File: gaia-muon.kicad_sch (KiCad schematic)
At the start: 88 parts, among them J1 Debug_Conn, J2 Conn_02x10_Odd_Even, J3 Conn_02x10_Odd_Even, J4 Conn_01x04_Pin, Q1 2N7002, SW1 SW_Push, U1 TPH2502, U2 TPH2502, U3 MAX5026, U4 LM4040DBZ-2.5, U5 MICROFC-60035-SIPM, U6 RP2040, U7 AP2112K-3.3, U8 W25Q128JVS, Y1 AMB8-272-T3

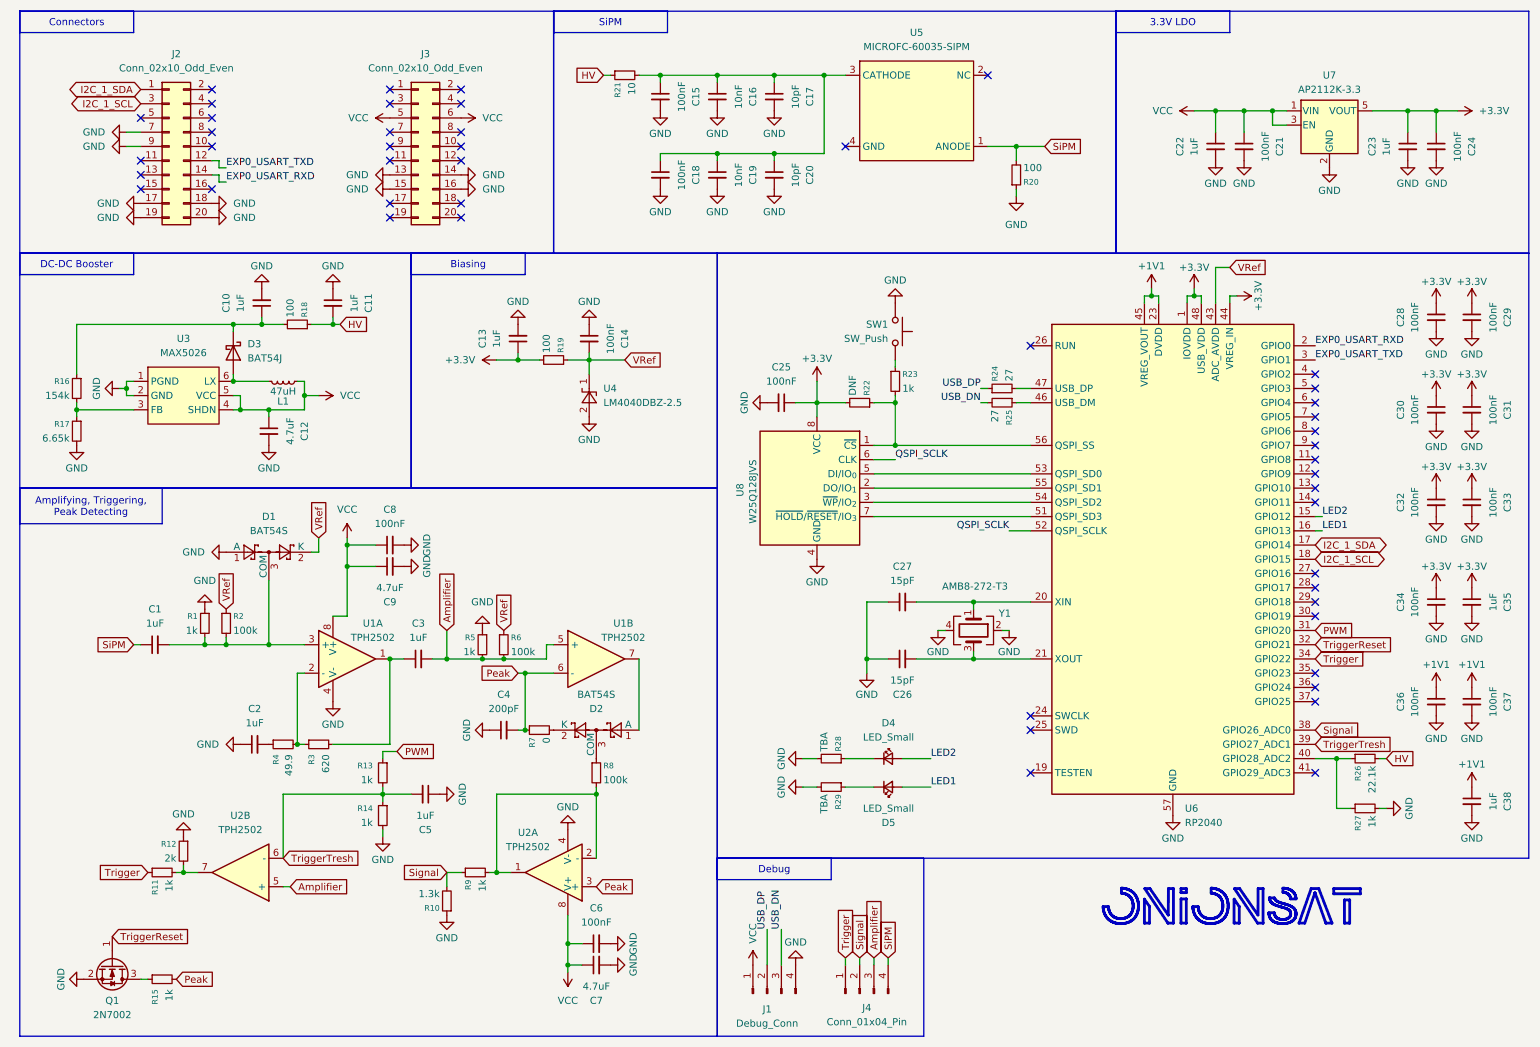
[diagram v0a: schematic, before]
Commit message: placing components, start routing
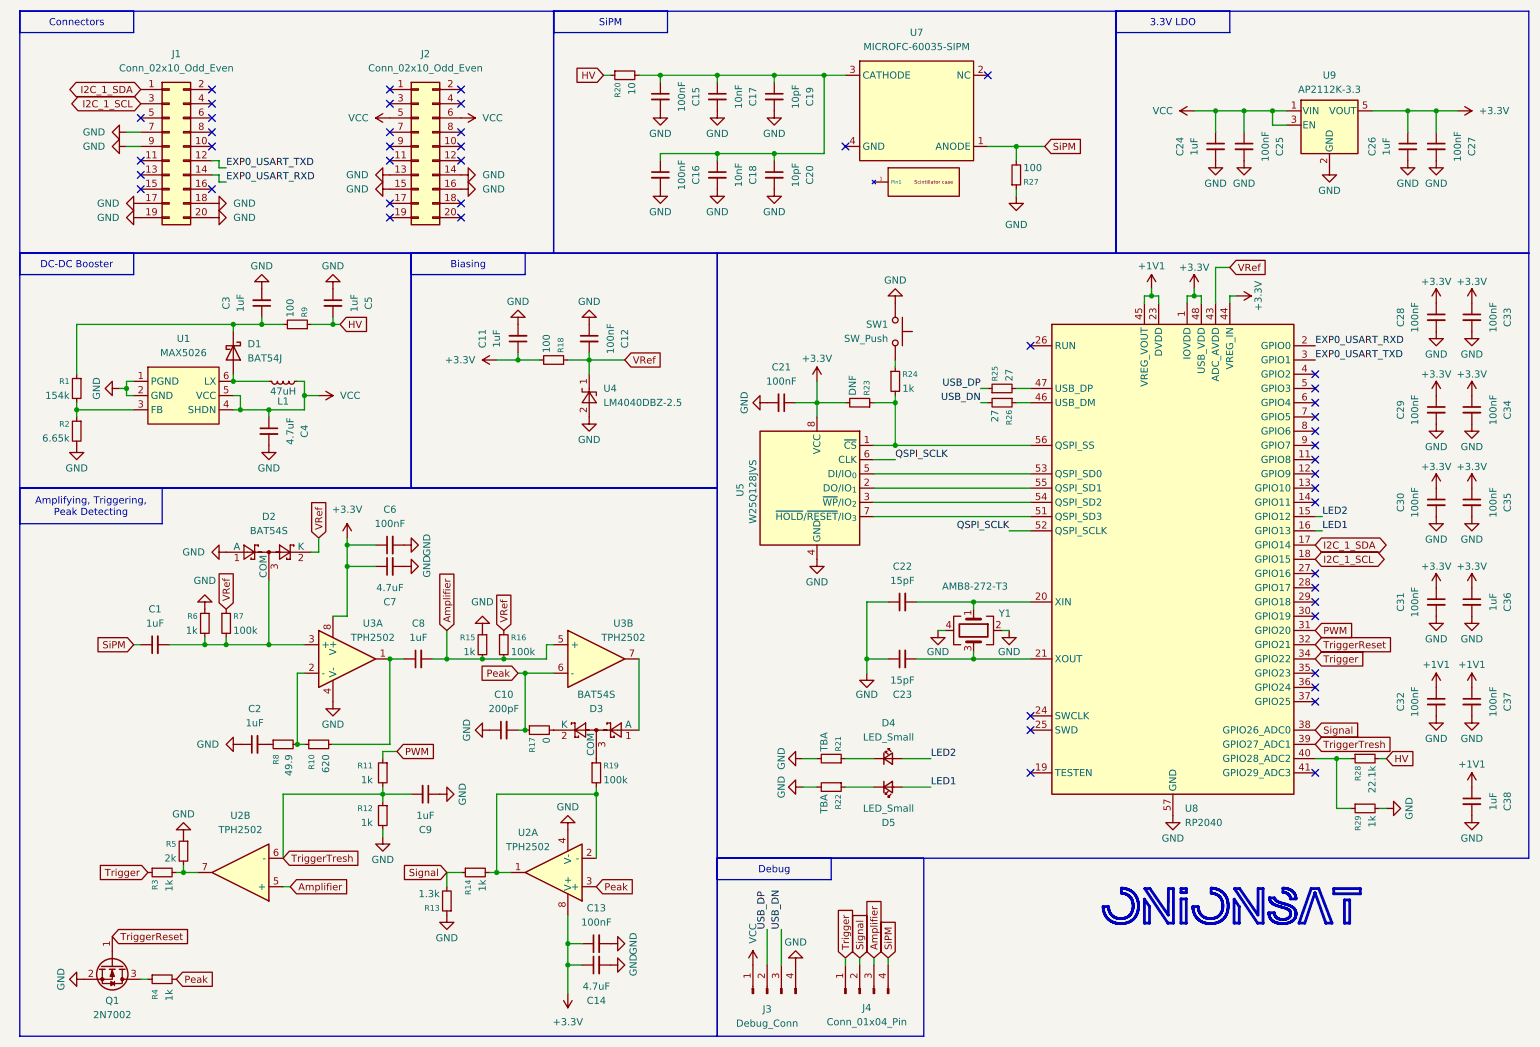
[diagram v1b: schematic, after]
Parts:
- added U6: ~, gaia-muon-footprints:scintillator-case, symbol gaia-muon-symbols:scintillator-case
- C1, C15, C2, C20: footprint (none) -> Capacitor_SMD:C_0805_2012Metric
- C10: renamed from C4; footprint (none) -> Capacitor_SMD:C_0805_2012Metric
- C11: renamed from C13; footprint (none) -> Capacitor_SMD:C_0805_2012Metric
- C12: renamed from C14; footprint (none) -> Capacitor_SMD:C_0805_2012Metric
- C13: renamed from C6; footprint (none) -> Capacitor_SMD:C_0402_1005Metric
- C14: renamed from C7; footprint (none) -> Capacitor_SMD:C_0402_1005Metric
- C16: renamed from C18; footprint (none) -> Capacitor_SMD:C_0805_2012Metric
- C17: renamed from C16; footprint (none) -> Capacitor_SMD:C_0805_2012Metric
- C18: renamed from C19; footprint (none) -> Capacitor_SMD:C_0805_2012Metric
- C19: renamed from C17; footprint (none) -> Capacitor_SMD:C_0805_2012Metric
- C21: renamed from C25; footprint (none) -> Capacitor_SMD:C_0805_2012Metric
- C22: renamed from C27; footprint (none) -> Capacitor_SMD:C_0402_1005Metric
- C23: renamed from C26; footprint (none) -> Capacitor_SMD:C_0402_1005Metric
- C24: renamed from C22; footprint (none) -> Capacitor_SMD:C_0603_1608Metric
- C25: renamed from C21; footprint (none) -> Capacitor_SMD:C_0603_1608Metric
- C26: renamed from C23; footprint (none) -> Capacitor_SMD:C_0603_1608Metric
- C27: renamed from C24; footprint (none) -> Capacitor_SMD:C_0603_1608Metric
- C28, C37, C38: footprint (none) -> Capacitor_SMD:C_0402_1005Metric
- C29: renamed from C30; footprint (none) -> Capacitor_SMD:C_0402_1005Metric
- C3: renamed from C10; footprint (none) -> Capacitor_SMD:C_0805_2012Metric
- C30: renamed from C32; footprint (none) -> Capacitor_SMD:C_0402_1005Metric
- C31: renamed from C34; footprint (none) -> Capacitor_SMD:C_0402_1005Metric
- C32: renamed from C36; footprint (none) -> Capacitor_SMD:C_0402_1005Metric
- C33: renamed from C29; footprint (none) -> Capacitor_SMD:C_0402_1005Metric
- C34: renamed from C31; footprint (none) -> Capacitor_SMD:C_0402_1005Metric
- C35: renamed from C33; footprint (none) -> Capacitor_SMD:C_0402_1005Metric
- C36: renamed from C35; footprint (none) -> Capacitor_SMD:C_0402_1005Metric
- C4: renamed from C12; footprint (none) -> Capacitor_SMD:C_0805_2012Metric
- C5: renamed from C11; footprint (none) -> Capacitor_SMD:C_0805_2012Metric
- C6: renamed from C8; footprint (none) -> Capacitor_SMD:C_0402_1005Metric
- C7: renamed from C9; footprint (none) -> Capacitor_SMD:C_0402_1005Metric
- C8: renamed from C3; footprint (none) -> Capacitor_SMD:C_0805_2012Metric
- C9: renamed from C5; footprint (none) -> Capacitor_SMD:C_0805_2012Metric
- D4, D5: footprint (none) -> LED_SMD:LED_0603_1608Metric
- J1: renamed from J2; footprint gaia_obc-footprints:PinHeader_2x10_P2.00mm_Vertical_SMD -> gaia-muon-footprints:Gaia_connector_2_4layer
- J2: renamed from J3; footprint gaia_obc-footprints:PinHeader_2x10_P2.00mm_Vertical_SMD -> gaia-muon-footprints:Gaia_connector_2_4layer
- J3: renamed from J1; footprint (none) -> Connector_PinHeader_2.54mm:PinHeader_1x04_P2.54mm_Vertical
- J4: footprint (none) -> Connector_PinHeader_2.54mm:PinHeader_1x04_P2.54mm_Vertical
- L1: footprint (none) -> Inductor_SMD:L_0805_2012Metric
- R1: renamed from R16; footprint (none) -> Resistor_SMD:R_0603_1608Metric
- R10: renamed from R3; footprint (none) -> Resistor_SMD:R_0805_2012Metric
- R11: renamed from R13; footprint (none) -> Resistor_SMD:R_0805_2012Metric
- R12: renamed from R14; footprint (none) -> Resistor_SMD:R_0805_2012Metric
- R13: renamed from R10; footprint (none) -> Resistor_SMD:R_0805_2012Metric
- R14: renamed from R9; footprint (none) -> Resistor_SMD:R_0805_2012Metric
- R15: renamed from R5; footprint (none) -> Resistor_SMD:R_0805_2012Metric
- R16: renamed from R6; footprint (none) -> Resistor_SMD:R_0805_2012Metric
- R17: renamed from R7; footprint (none) -> Resistor_SMD:R_0805_2012Metric
- R18: renamed from R19; footprint (none) -> Resistor_SMD:R_0805_2012Metric
- R19: renamed from R8; footprint (none) -> Resistor_SMD:R_0805_2012Metric
- R2: renamed from R17; footprint (none) -> Resistor_SMD:R_0603_1608Metric
- R20: renamed from R21; footprint (none) -> Resistor_SMD:R_0805_2012Metric
- R21: renamed from R28; footprint (none) -> Resistor_SMD:R_0402_1005Metric
- R22: renamed from R29; footprint (none) -> Resistor_SMD:R_0402_1005Metric
- R23: renamed from R22; footprint (none) -> Resistor_SMD:R_0402_1005Metric
- R24: renamed from R23; footprint (none) -> Resistor_SMD:R_0402_1005Metric
- R25: renamed from R24; footprint (none) -> Resistor_SMD:R_0402_1005Metric
- R26: renamed from R25; footprint (none) -> Resistor_SMD:R_0402_1005Metric
- R27: renamed from R20; footprint (none) -> Resistor_SMD:R_0805_2012Metric
- R28: renamed from R26; footprint (none) -> Resistor_SMD:R_0805_2012Metric
- R29: renamed from R27; footprint (none) -> Resistor_SMD:R_0805_2012Metric
- R3: renamed from R11; footprint (none) -> Resistor_SMD:R_0805_2012Metric
- R4: renamed from R15; footprint (none) -> Resistor_SMD:R_0805_2012Metric
- R5: renamed from R12; footprint (none) -> Resistor_SMD:R_0805_2012Metric
- R6: renamed from R1; footprint (none) -> Resistor_SMD:R_0805_2012Metric
- R7: renamed from R2; footprint (none) -> Resistor_SMD:R_0805_2012Metric
- R8: renamed from R4; footprint (none) -> Resistor_SMD:R_0805_2012Metric
- R9: renamed from R18; footprint (none) -> Resistor_SMD:R_0805_2012Metric
- SW1: footprint (none) -> gaia-muon-footprints:KEY-SMD_L4.0-W3.0-LS4.9-1
- U1: renamed from U3; footprint (none) -> Package_TO_SOT_SMD:SOT-23-6
- U3: renamed from U1; footprint Package_SO:SOP-8_3.76x4.96mm_P1.27mm -> Package_SO:MSOP-8_3x3mm_P0.65mm
- U7: renamed from U5; footprint (none) -> gaia-muon-footprints:MICROFC-60035-SIPM
- renumbered D3 to D1, D1 to D2, D2 to D3, U8 to U5, U6 to U8, U7 to U9
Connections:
- net +3.3V: now also C13.1, C14.1, C6.1, C7.1, U2.8 (V+), U3.8 (V+)
- net VCC: no longer C13.1, C14.1, C6.1, C7.1, U2.8 (V+), U3.8 (V+)

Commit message: silkscreen cleanup
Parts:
- D2, D3, Q1, U4: footprint Package_TO_SOT_SMD:SOT-23 -> gaia-muon-footprints:SOT-23
- J3, J4: footprint Connector_PinHeader_2.54mm:PinHeader_1x04_P2.54mm_Vertical -> gaia-muon-footprints:PinHeader_1x04_P2.54mm_Vertical
- U1: footprint Package_TO_SOT_SMD:SOT-23-6 -> gaia-muon-footprints:SOT-23-6
- U2, U3: footprint Package_SO:MSOP-8_3x3mm_P0.65mm -> gaia-muon-footprints:MSOP-8_3x3mm_P0.65mm
- U5: footprint Package_SO:SOIC-8_5.3x5.3mm_P1.27mm -> gaia-muon-footprints:SOIC-8_5.3x5.3mm_P1.27mm
- U8: footprint Package_DFN_QFN:QFN-56-1EP_7x7mm_P0.4mm_EP3.2x3.2mm -> gaia-muon-footprints:QFN-56-1EP_7x7mm_P0.4mm_EP3.2x3.2mm
- U9: footprint Package_TO_SOT_SMD:SOT-23-5 -> gaia-muon-footprints:SOT-23-5
- Y1: footprint Crystal:Crystal_SMD_3225-4Pin_3.2x2.5mm -> gaia-muon-footprints:Crystal_SMD_3225-4Pin_3.2x2.5mm
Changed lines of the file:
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@@
 			)
 		)
-		(property "Footprint" "Crystal:Crystal_SMD_3225-4Pin_3.2x2.5mm"
+		(property "Footprint" "gaia-muon-footprints:Crystal_SMD_3225-4Pin_3.2x2.5mm"
 			(at 184.15 124.46 0)
 			(effects
@@
 			)
 		)
-		(property "Footprint" "Connector_PinHeader_2.54mm:PinHeader_1x04_P2.54mm_Vertical"
+		(property "Footprint" "gaia-muon-footprints:PinHeader_1x04_P2.54mm_Vertical"
 			(at 163.83 189.23 0)
 			(effects
@@
 			)
 		)
-		(property "Footprint" "Package_SO:MSOP-8_3x3mm_P0.65mm"
+		(property "Footprint" "gaia-muon-footprints:MSOP-8_3x3mm_P0.65mm"
 			(at 53.34 167.64 0)
 			(effects
@@
 			)
 		)
-		(property "Footprint" "Package_TO_SOT_SMD:SOT-23"
+		(property "Footprint" "gaia-muon-footprints:SOT-23"
 			(at 120.65 82.55 0)
 			(effects
@@
 			)
 		)
-		(property "Footprint" "Package_TO_SOT_SMD:SOT-23"
+		(property "Footprint" "gaia-muon-footprints:SOT-23"
 			(at 28.575 189.23 0)
 			(effects
@@
 			)
 		)
-		(property "Footprint" "Package_TO_SOT_SMD:SOT-23-6"
+		(property "Footprint" "gaia-muon-footprints:SOT-23-6"
 			(at 43.18 81.28 0)
 			(effects
@@
 			)
 		)
-		(property "Footprint" "Package_SO:MSOP-8_3x3mm_P0.65mm"
+		(property "Footprint" "gaia-muon-footprints:MSOP-8_3x3mm_P0.65mm"
 			(at 116.84 129.54 0)
 			(effects
@@
 			)
 		)
-		(property "Footprint" "Package_TO_SOT_SMD:SOT-23"
+		(property "Footprint" "gaia-muon-footprints:SOT-23"
 			(at 114.935 139.065 0)
 			(effects
@@
 			)
 		)
-		(property "Footprint" "Package_SO:MSOP-8_3x3mm_P0.65mm"
+		(property "Footprint" "gaia-muon-footprints:MSOP-8_3x3mm_P0.65mm"
 			(at 72.39 129.54 0)
 			(effects
@@
 			)
 		)
-		(property "Footprint" "Package_TO_SOT_SMD:SOT-23"
+		(property "Footprint" "gaia-muon-footprints:SOT-23"
 			(at 60.325 107.315 0)
 			(effects
@@
 			)
 		)
-		(property "Footprint" "Package_DFN_QFN:QFN-56-1EP_7x7mm_P0.4mm_EP3.2x3.2mm"
+		(property "Footprint" "gaia-muon-footprints:QFN-56-1EP_7x7mm_P0.4mm_EP3.2x3.2mm"
 			(at 219.71 111.76 0)
 			(effects
@@
 			)
 		)
-		(property "Footprint" "Package_SO:MSOP-8_3x3mm_P0.65mm"
+		(property "Footprint" "gaia-muon-footprints:MSOP-8_3x3mm_P0.65mm"
 			(at 72.39 129.54 0)
 			(effects
@@
 			)
 		)
-		(property "Footprint" "Connector_PinHeader_2.54mm:PinHeader_1x04_P2.54mm_Vertical"
+		(property "Footprint" "gaia-muon-footprints:PinHeader_1x04_P2.54mm_Vertical"
 			(at 147.32 189.23 0)
 			(effects
@@
 			)
 		)
-		(property "Footprint" "Package_TO_SOT_SMD:SOT-23-5"
+		(property "Footprint" "gaia-muon-footprints:SOT-23-5"
 			(at 247.65 26.035 0)
 			(effects
@@
 			)
 		)
-		(property "Footprint" "Package_SO:SOIC-8_5.3x5.3mm_P1.27mm"
+		(property "Footprint" "gaia-muon-footprints:SOIC-8_5.3x5.3mm_P1.27mm"
 			(at 156.21 76.2 0)
 			(effects
@@
 			)
 		)
-		(property "Footprint" "Package_SO:MSOP-8_3x3mm_P0.65mm"
+		(property "Footprint" "gaia-muon-footprints:MSOP-8_3x3mm_P0.65mm"
 			(at 109.22 167.64 0)
 			(effects
@@
 			)
 		)
-		(property "Footprint" "Package_SO:MSOP-8_3x3mm_P0.65mm"
+		(property "Footprint" "gaia-muon-footprints:MSOP-8_3x3mm_P0.65mm"
 			(at 109.22 167.64 0)
 			(effects
